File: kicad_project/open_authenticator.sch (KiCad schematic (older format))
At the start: 52 parts, among them IC1 TPS22919DCKR, J1 Conn_01x02_Female, J2 TYPE-C-31-M-17, J3 Conn_01x02_Female, Q1 DMP2305U-7, SW1 UP, SW2 DOWN, SW3 BOOT/SELECT, SW4 RESET, SW5 POWER SWITCH, U1 ESP32-WROOM-32, U2 DS3231M, U3 MCP73831-2-OT, U4 TPS63001

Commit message: renamed kicad project
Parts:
- BT1: symbol esp_2fa_board_design-rescue:Battery_Cell-Device-esp_2fa_board_design-rescue -> open_authenticator-rescue:Battery_Cell-Device-esp_2fa_board_design-rescue-esp_2fa_board_design-rescue-open_authenticato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
- C1, C10, C11, C2, C3, C4, C5, C6, C7, C8, C9: symbol esp_2fa_board_design-rescue:C-Device-esp_2fa_board_design-rescue -> open_authenticator-rescue:C-Device-esp_2fa_board_design-rescue-esp_2fa_board_design-rescue-open_authenticator-rescue
- D2: symbol esp_2fa_board_design-rescue:LED-Device-esp_2fa_board_design-rescue -> open_authenticator-rescue:LED-Device-esp_2fa_board_design-rescue-esp_2fa_board_design-rescue-open_authenticator-rescue
- D3: symbol esp_2fa_board_design-rescue:1N5819-Diode-esp_2fa_board_design-rescue -> open_authenticator-rescue:1N5819-Diode-esp_2fa_board_design-rescue-esp_2fa_board_design-rescue-open_authenticator-rescue
- L1: symbol esp_2fa_board_design-rescue:INDUCTOR-pspice-esp_2fa_board_design-rescue -> open_authenticator-rescue:INDUCTOR-pspice-esp_2fa_board_design-rescue-esp_2fa_board_design-rescue-open_authenticator-re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
- R1, R10, R11, R12, R13, R14, R2, R3, R4, R5, R6, R7, R8, R9: symbol esp_2fa_board_design-rescue:R_Small_US-Device-esp_2fa_board_design-rescue -> open_authenticator-rescue:R_Small_US-Device-esp_2fa_board_design-rescue-esp_2fa_board_design-rescue-open_authenticator-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
- SW1, SW2, SW3, SW4: symbol esp_2fa_board_design-rescue:SW_Push-Switch-esp_2fa_board_design-rescue -> open_authenticator-rescue:SW_Push-Switch-esp_2fa_board_design-rescue-esp_2fa_board_design-rescue-open_authenticator-res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
- U1: symbol esp_2fa_board_design-rescue:ESP32-WROOM-32-RF_Module-esp_2fa_board_design-rescue -> open_authenticator-rescue:ESP32-WROOM-32-RF_Module-esp_2fa_board_design-rescue-esp_2fa_board_design-rescue-open_authent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
- U2: symbol esp_2fa_board_design-rescue:DS3231M-Timer_RTC-esp_2fa_board_design-rescue -> open_authenticator-rescue:DS3231M-Timer_RTC-esp_2fa_board_design-rescue-esp_2fa_board_design-rescue-open_authenticator-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
- U3: symbol esp_2fa_board_design-rescue:MCP73831-2-OT-Battery_Management-esp_2fa_board_design-rescue -> open_authenticator-rescue:MCP73831-2-OT-Battery_Management-esp_2fa_board_design-rescue-esp_2fa_board_design-rescue-open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
- U4: symbol esp_2fa_board_design-rescue:TPS63001-Regulator_Switching-esp_2fa_board_design-rescue -> open_authenticator-rescue:TPS63001-Regulator_Switching-esp_2fa_board_design-rescue-esp_2fa_board_design-rescue-open_aut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

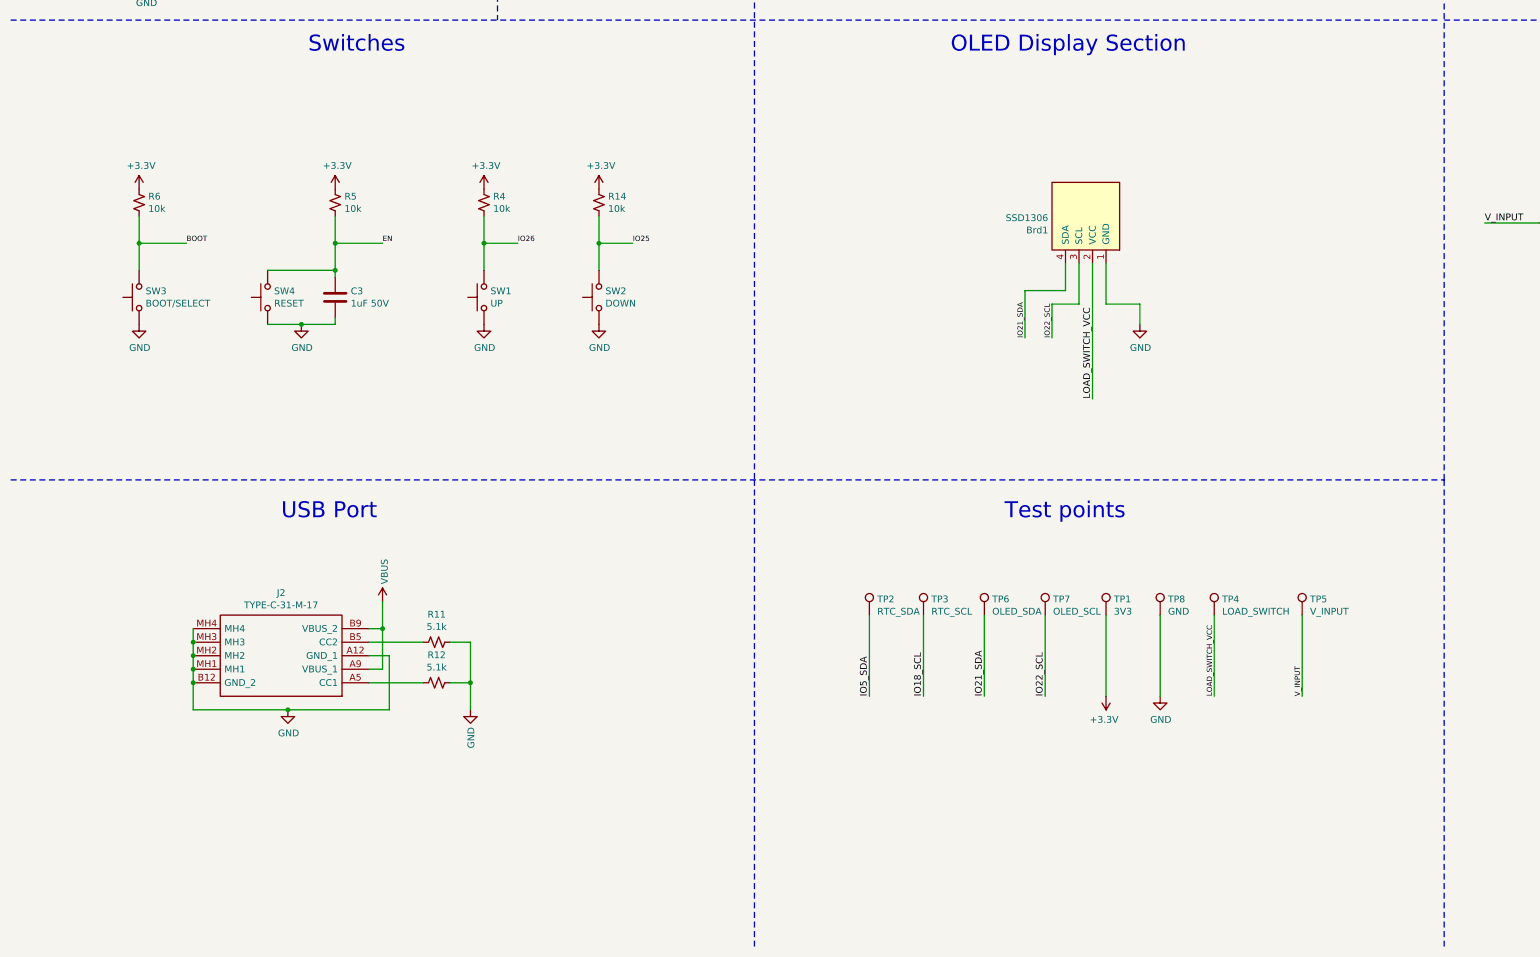
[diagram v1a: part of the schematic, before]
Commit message: Added 3D-models of majority components and added schematics of bare oled-panel, assigned footprints, routing is to be done
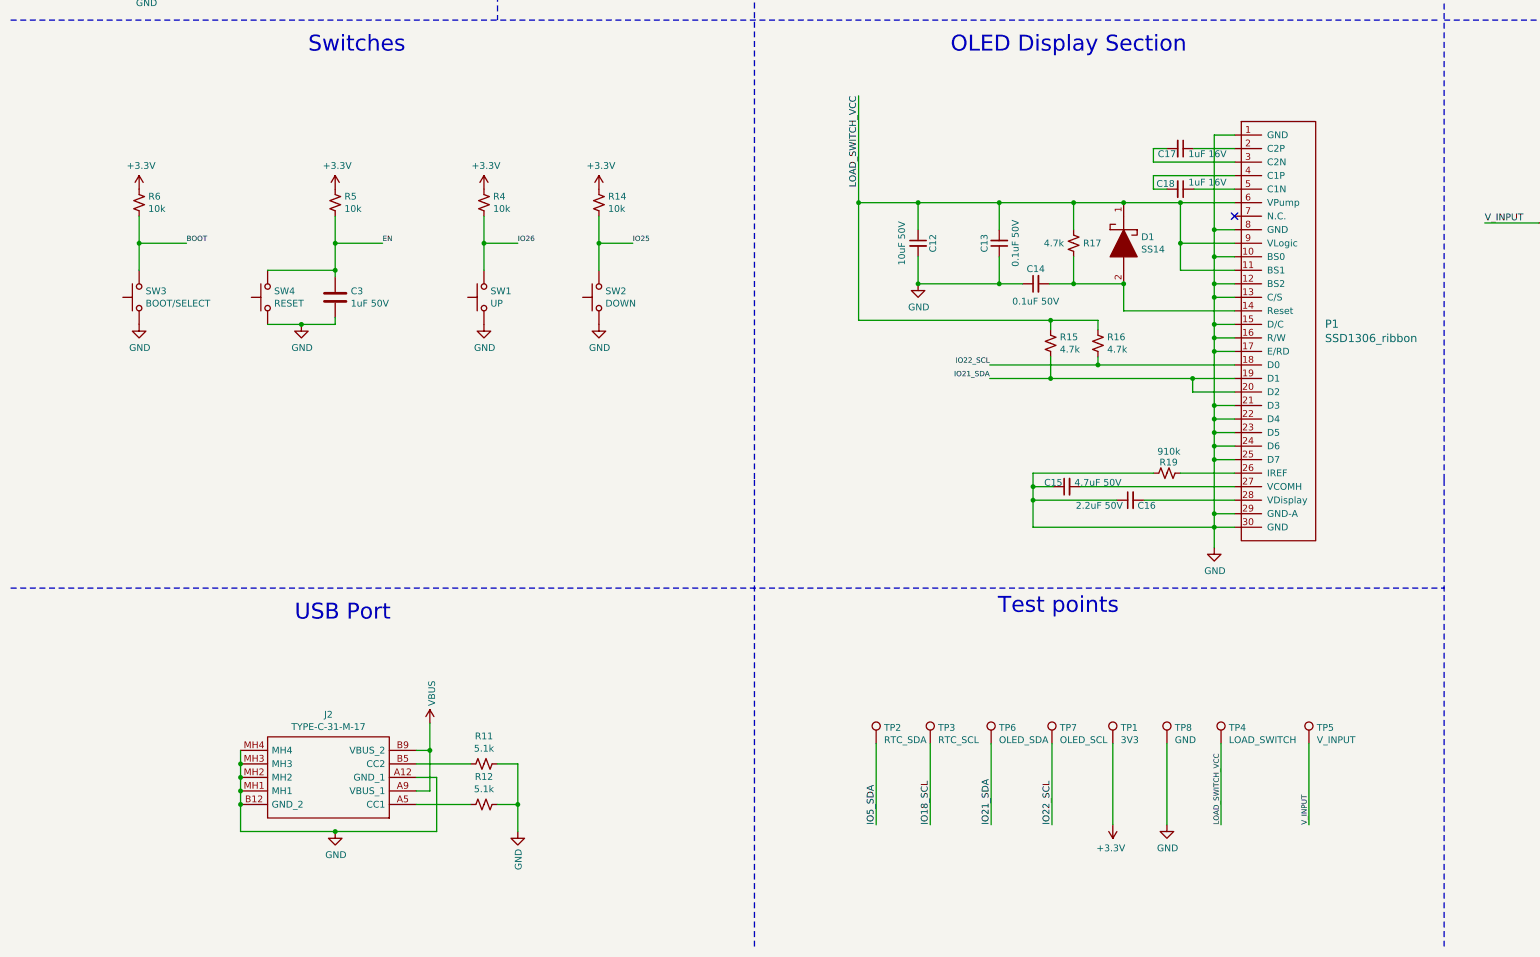
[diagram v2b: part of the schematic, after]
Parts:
- removed Brd1: SSD1306, SSD1306:128x64OLED, symbol SSD1306-128x64_OLED:SSD1306
- added C12: 10uF 50V, Capacitor_SMD:C_1206_3216Metric, symbol Device:C_Small
- added C13, C14: 0.1uF 50V, Capacitor_SMD:C_1206_3216Metric, symbol Device:C_Small
- added C15: 4.7uF 50V, Capacitor_SMD:C_1206_3216Metric, symbol Device:C_Small
- added C16: 2.2uF 50V, Capacitor_SMD:C_1206_3216Metric, symbol Device:C_Small
- added C17, C18: 1uF 16V, Capacitor_SMD:C_1206_3216Metric, symbol Device:C_Small
- added D1: SS14, SS14:DIOM5227X270N, symbol SS14:SS14
- added P1: SSD1306_ribbon, ribbon_connectors:SSD1306_ribbon, symbol oled_ribbon_connectors:SSD1306_ribbon
- added R15, R16, R17: 4.7k, Resistor_SMD:R_0603_1608Metric, symbol open_authenticator-rescue:R_Small_US-Device-esp_2fa_board_design-rescue-esp_2fa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
- added R19: 910k, Resistor_SMD:R_0603_1608Metric, symbol open_authenticator-rescue:R_Small_US-Device-esp_2fa_board_design-rescue-esp_2fa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
- BT1: footprint BU2032SM-BT-GTR:BU2032SMBTGTR -> CR2032-BS-6-1:CR2032BS61
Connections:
- net GND: now also C12.2, C13.1, C14.1, C15.1, C16.1, P1.1 (GND), P1.10 (BS0), P1.12 (BS2), P1.13 (C/S), P1.15 (D/C), P1.16 (R/W), P1.17 (E/RD), P1.21 (D3), P1.22 (D4), P1.23 (D5), P1.24 (D6), P1.25 (D7), P1.29 (GND-A), P1.30 (GND), P1.8 (GND), R19.1
- net IO21_SDA: now also P1.19 (D1), P1.20 (D2), R15.2
- net IO22_SCL: now also P1.18 (D0), R16.2
- net LOAD_SWITCH_VCC: now also C12.1, C13.2, D1.1, P1.11 (BS1), P1.6 (VPump), P1.9 (VLogic), R15.1, R16.1, R17.1
- new net: C14.2, D1.2, P1.14 (Reset), R17.2
- new net: C17.1, P1.2 (C2P)
- new net: P1.26 (IREF), R19.2
- new net: C15.2, P1.27 (VCOMH)
- new net: C16.2, P1.28 (VDisplay)
- new net: C17.2, P1.3 (C2N)
- new net: C18.2, P1.4 (C1P)
- new net: C18.1, P1.5 (C1N)
- no-connect marks 25 -> 26
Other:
- moved on the sheet: J2, R11, R12, TP1, TP2, TP3, TP4, TP5, TP6, TP7, TP8

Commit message: Changed footprints of capacitors used in OLED sub circuit
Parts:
- C12: value 10uF 50V -> 10uF 16V; footprint Capacitor_SMD:C_1206_3216Metric -> Capacitor_SMD:C_0603_1608Metric
- C13, C14: value 0.1uF 50V -> 0.1uF 16V; footprint Capacitor_SMD:C_1206_3216Metric -> Capacitor_SMD:C_0603_1608Metric
- C15: value 4.7uF 50V -> 4.7uF 16V; footprint Capacitor_SMD:C_1206_3216Metric -> Capacitor_SMD:C_0603_1608Metric
- C16: value 2.2uF 50V -> 2.2uF 16V; footprint Capacitor_SMD:C_1206_3216Metric -> Capacitor_SMD:C_0603_1608Metric
- C17, C18: footprint Capacitor_SMD:C_1206_3216Metric -> Capacitor_SMD:C_0603_1608Metric
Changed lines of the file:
@@
 F 0 "C18" V 9160 5440 50  0000 C CNN
 F 1 "1uF 16V" V 9150 5750 50  0000 C CNN
-F 2 "Capacitor_SMD:C_1206_3216Metric" H 9200 5550 50  0001 C CNN
+F 2 "Capacitor_SMD:C_0603_1608Metric" H 9200 5550 50  0001 C CNN
 F 3 "~" H 9200 5550 50  0001 C CNN
 	1    9200 5550
@@
 F 0 "C17" V 9240 5150 50  0000 C CNN
 F 1 "1uF 16V" V 9240 5450 50  0000 C CNN
-F 2 "Capacitor_SMD:C_1206_3216Metric" H 9200 5250 50  0001 C CNN
+F 2 "Capacitor_SMD:C_0603_1608Metric" H 9200 5250 50  0001 C CNN
 F 3 "~" H 9200 5250 50  0001 C CNN
 	1    9200 5250
@@
 P 7260 5950
 F 0 "C12" V 7370 5950 50  0000 C CNN
-F 1 "10uF 50V" V 7140 5950 50  0000 C CNN
-F 2 "Capacitor_SMD:C_1206_3216Metric" H 7260 5950 50  0001 C CNN
+F 1 "10uF 16V" V 7140 5950 50  0000 C CNN
+F 2 "Capacitor_SMD:C_0603_1608Metric" H 7260 5950 50  0001 C CNN
 F 3 "~" H 7260 5950 50  0001 C CNN
 	1    7260 5950
@@
 P 7860 5950
 F 0 "C13" V 7970 5950 50  0000 C CNN
-F 1 "0.1uF 50V" V 7740 5950 50  0000 C CNN
-F 2 "Capacitor_SMD:C_1206_3216Metric" H 7860 5950 50  0001 C CNN
+F 1 "0.1uF 16V" V 7740 5950 50  0000 C CNN
+F 2 "Capacitor_SMD:C_0603_1608Metric" H 7860 5950 50  0001 C CNN
 F 3 "~" H 7860 5950 50  0001 C CNN
 	1    7860 5950
@@
 P 8130 6250
 F 0 "C14" V 8240 6250 50  0000 C CNN
-F 1 "0.1uF 50V" V 8000 6250 50  0000 C CNN
-F 2 "Capacitor_SMD:C_1206_3216Metric" H 8130 6250 50  0001 C CNN
+F 1 "0.1uF 16V" V 8000 6250 50  0000 C CNN
+F 2 "Capacitor_SMD:C_0603_1608Metric" H 8130 6250 50  0001 C CNN
 F 3 "~" H 8130 6250 50  0001 C CNN
 	1    8130 6250
@@
 P 8360 7750
 F 0 "C15" V 8390 7850 50  0000 C CNN
-F 1 "4.7uF 50V" V 8390 7520 50  0000 C CNN
-F 2 "Capacitor_SMD:C_1206_3216Metric" H 8360 7750 50  0001 C CNN
+F 1 "4.7uF 16V" V 8390 7520 50  0000 C CNN
+F 2 "Capacitor_SMD:C_0603_1608Metric" H 8360 7750 50  0001 C CNN
 F 3 "~" H 8360 7750 50  0001 C CNN
 	1    8360 7750
@@
 P 8830 7850
 F 0 "C16" V 8790 7730 50  0000 C CNN
-F 1 "2.2uF 50V" V 8790 8080 50  0000 C CNN
-F 2 "Capacitor_SMD:C_1206_3216Metric" H 8830 7850 50  0001 C CNN
+F 1 "2.2uF 16V" V 8790 8080 50  0000 C CNN
+F 2 "Capacitor_SMD:C_0603_1608Metric" H 8830 7850 50  0001 C CNN
 F 3 "~" H 8830 7850 50  0001 C CNN
 	1    8830 7850

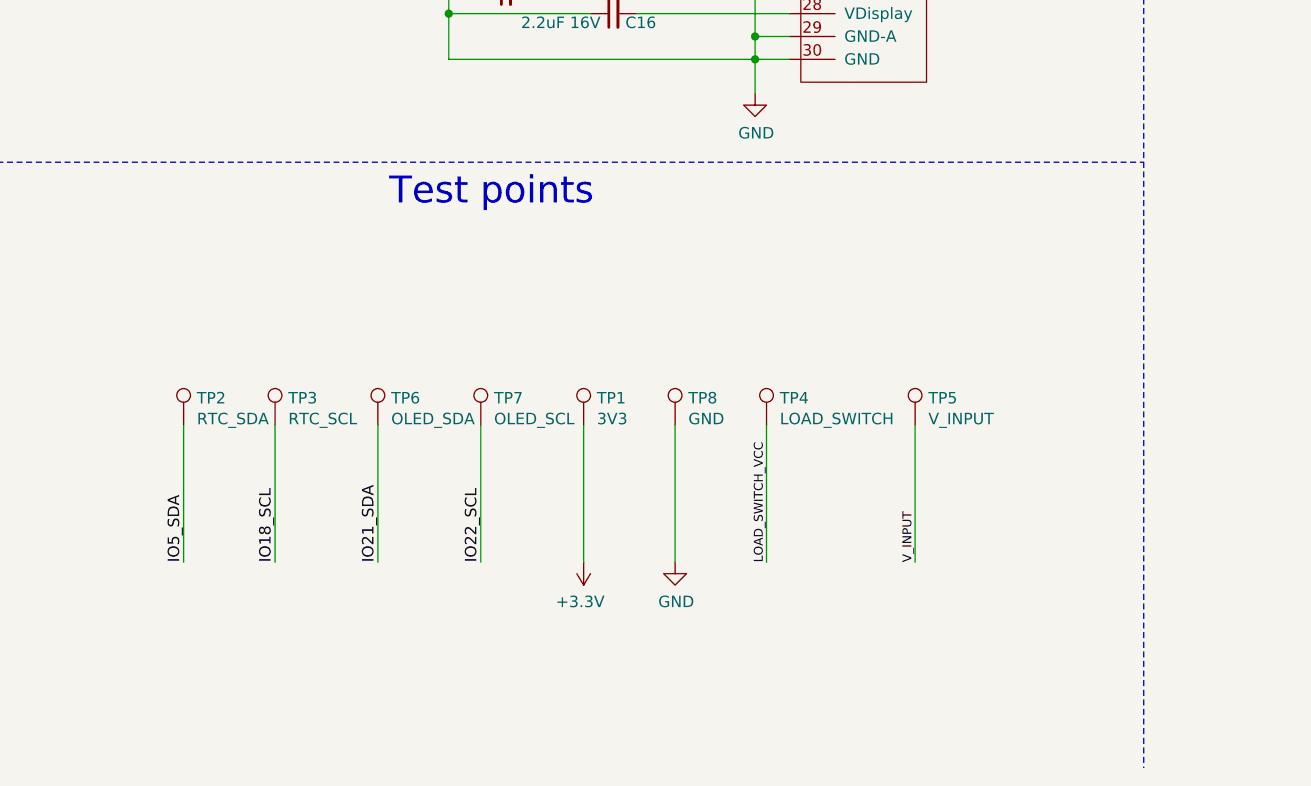
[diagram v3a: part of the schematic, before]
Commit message: Added mounting holes in schematics
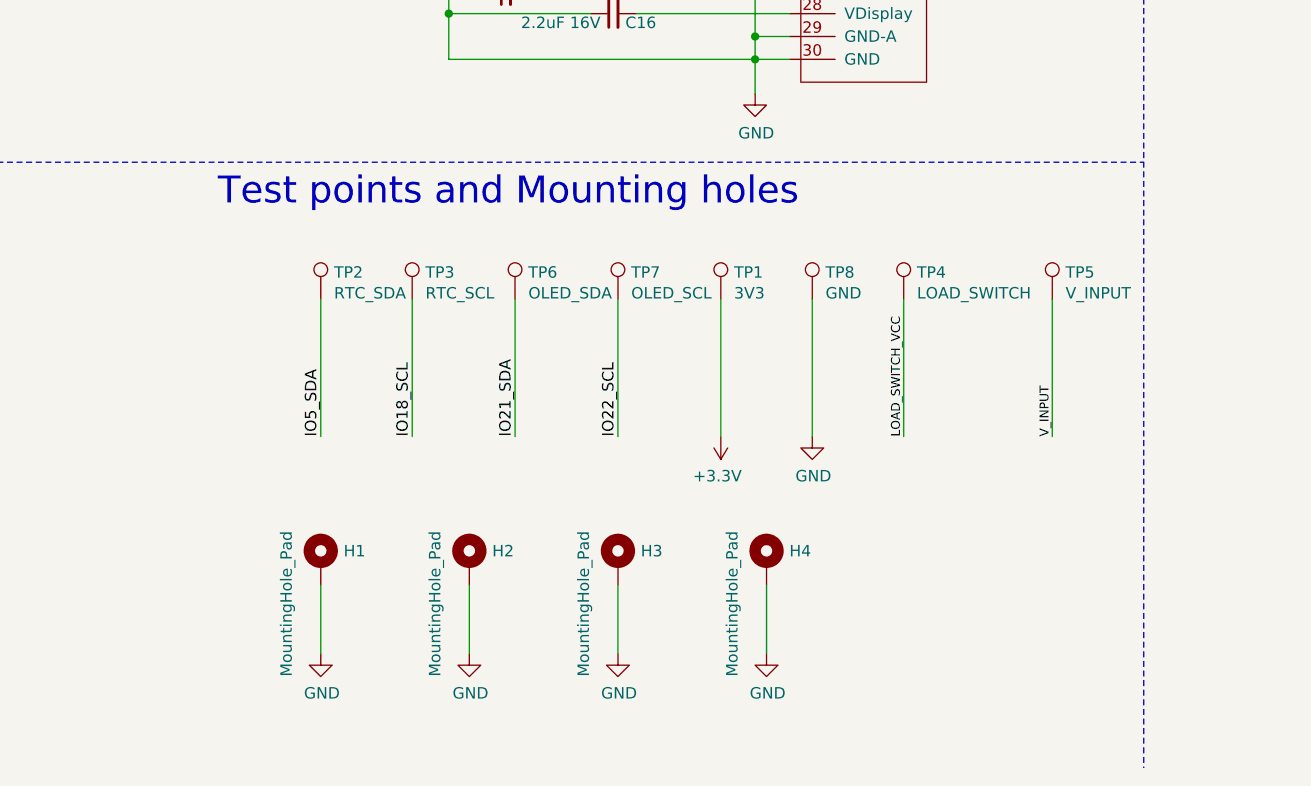
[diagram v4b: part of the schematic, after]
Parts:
- added H1, H2, H3, H4: MountingHole_Pad, MountingHole:MountingHole_2.2mm_M2_ISO7380_Pad, symbol Mechanical:MountingHole_Pad
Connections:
- net GND: now also H1.1, H2.1, H3.1, H4.1
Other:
- note added: "Test points and Mounting holes"
- note removed: "Test points"
- moved on the sheet: TP1, TP2, TP3, TP4, TP5, TP6, TP7, TP8

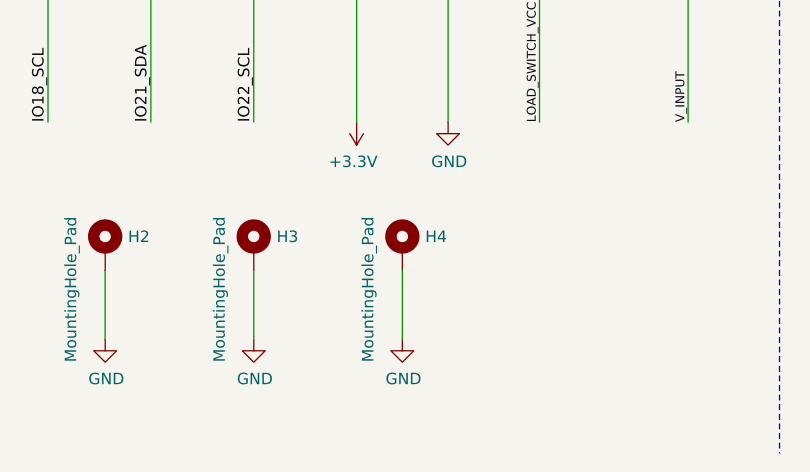
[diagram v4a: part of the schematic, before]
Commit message: Placed mounting holes on the board
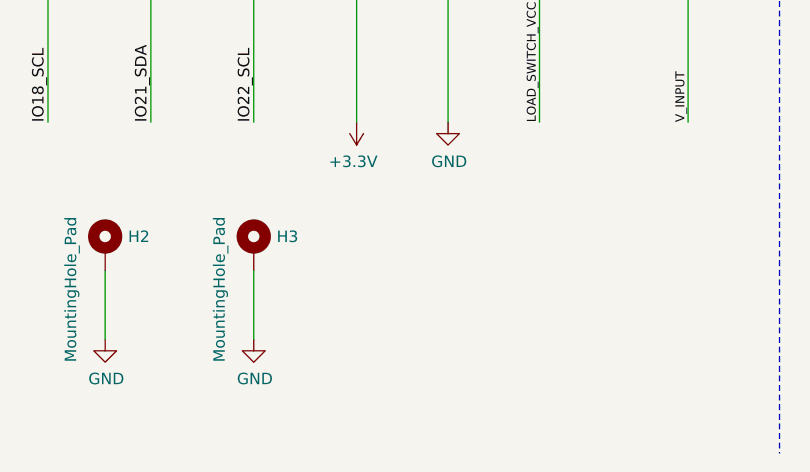
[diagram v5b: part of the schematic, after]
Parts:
- removed H4: MountingHole_Pad, MountingHole:MountingHole_2.2mm_M2_ISO7380_Pad, symbol Mechanical:MountingHole_Pad
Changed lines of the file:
@@
-$EndComp
-$Comp
-L Mechanical:MountingHole_Pad H4
-U 1 1 600C9E06
-P 9500 10250
-F 0 "H4" H 9600 10299 50  0000 L CNN
-F 1 "MountingHole_Pad" V 9350 9750 50  0000 L CNN
-F 2 "MountingHole:MountingHole_2.2mm_M2_ISO7380_Pad" H 9500 10250 50  0001 C CNN
-F 3 "~" H 9500 10250 50  0001 C CNN
-	1    9500 10250
-	1    0    0    -1
 $EndComp
 $Comp
@@
 Wire Wire Line
 	8850 10350 8850 10650
-$Comp
-L power:GND #PWR0104
-U 1 1 6019CA77
-P 9500 10650
-F 0 "#PWR0104" H 9500 10400 50  0001 C CNN
-F 1 "GND" H 9505 10477 50  0000 C CNN
-F 2 "" H 9500 10650 50  0001 C CNN
-F 3 "" H 9500 10650 50  0001 C CNN
-	1    9500 10650
-	1    0    0    -1
-$EndComp
-Wire Wire Line
-	9500 10350 9500 10650
 $EndSCHEMATC
